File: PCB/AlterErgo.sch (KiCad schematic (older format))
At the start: 85 parts, among them SW0:10 SW_Push, SW0:11 SW_Push, SW0:12 SW_Push, SW0:7 SW_Push, SW0:8 SW_Push, SW0:9 SW_Push, SW1:10 SW_Push, SW1:11 SW_Push, SW1:12 SW_Push, SW1:13 SW_Push, SW1:7 SW_Push, SW1:8 SW_Push, SW1:9 SW_Push, SW2:10 SW_Push, SW2:11 SW_Push, SW2:12 SW_Push, SW2:13 SW_Push, SW2:7 SW_Push, SW2:8 SW_Push, SW2:9 SW_Push, SW3:10 SW_Push, SW3:11 SW_Push, SW3:12 SW_Push, SW3:13 SW_Push, SW3:8 SW_Push, SW3:9 SW_Push, SW4:10 SW_Push, SW4:11 SW_Push, SW4:12 SW_Push, SW4:13 SW_Push, SW4:7 SW_Push, SW4:8 SW_Push, SW4:9 SW_Push, SW5:10 SW_Push, SW5:11 SW_Push, SW5:12 SW_Push, SW5:13 SW_Push, SW5:7 SW_Push, SW5:8 SW_Push, SW5:9 SW_Push

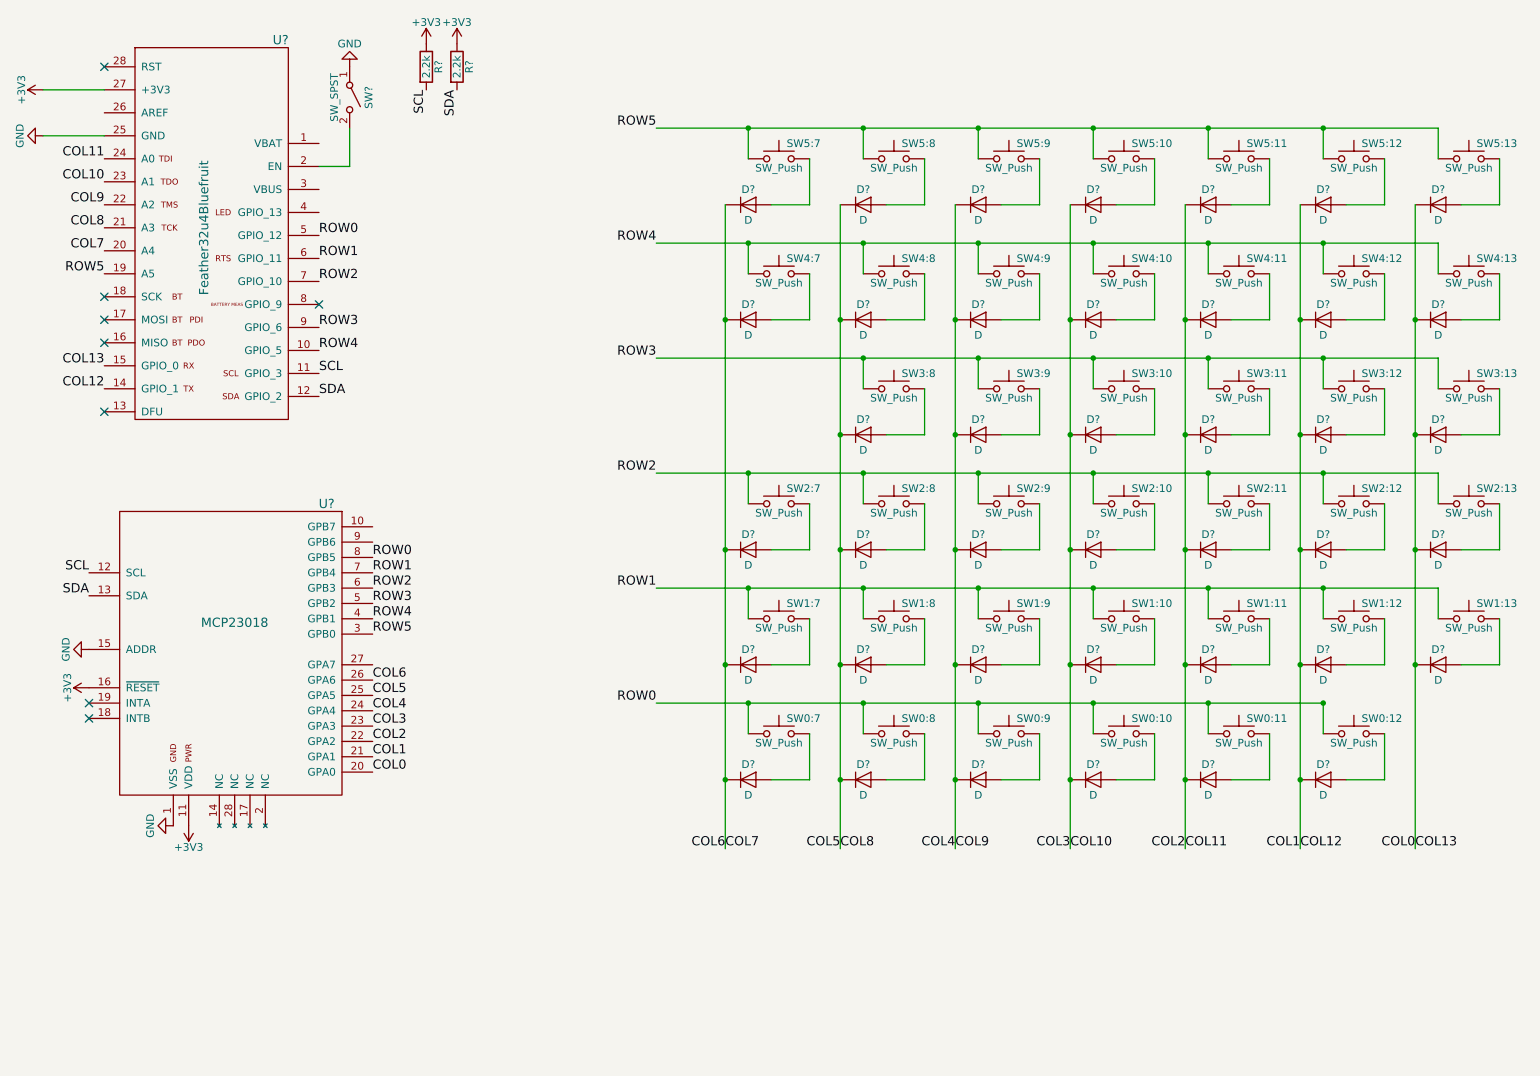
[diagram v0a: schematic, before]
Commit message: Add TRRS jack to schematic; annotate matrix diodes
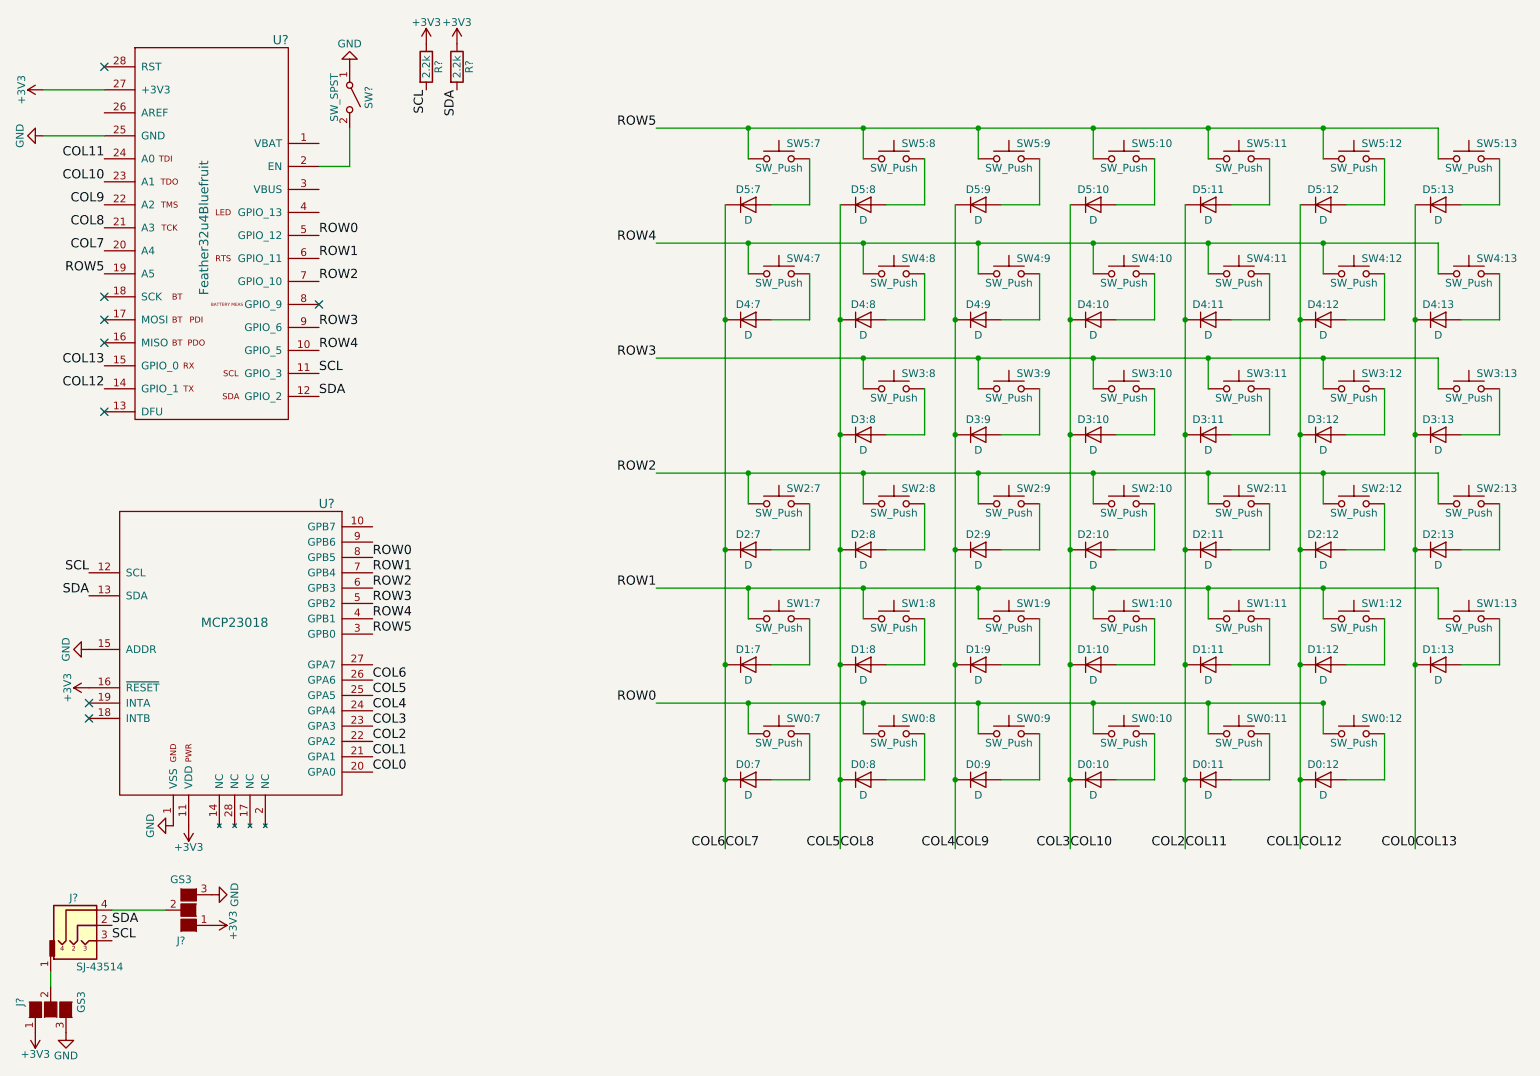
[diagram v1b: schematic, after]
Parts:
- added J?: SJ-43514, symbol SJ-43514
- added J? (x2): GS3, Connectors:GS3, symbol GS3
- gave numbers to parts that had none: 40
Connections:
- net +3V3: now also J?.1 (G1), J?.1 (G1)
- net GND: now also J?.3 (G3), J?.3 (G3)
- net SCL: now also J?.3
- net SDA: now also J?.2
- new net: J?.1, J?.2 (G2)
- new net: J?.2 (G2), J?.4

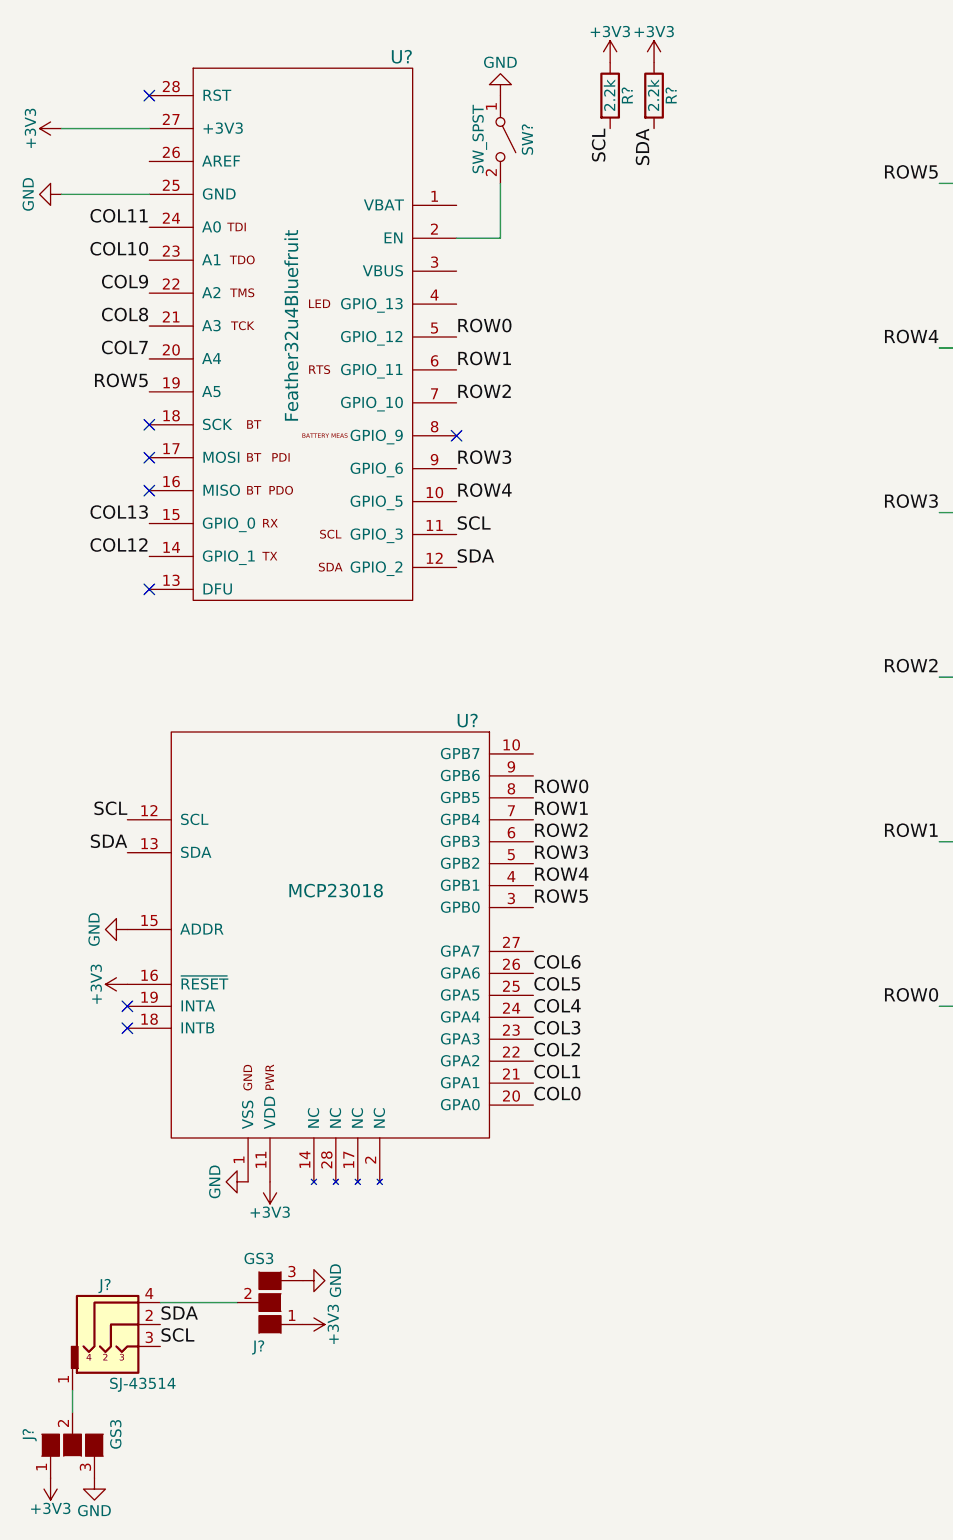
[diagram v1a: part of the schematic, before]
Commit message: Associate most components with footprints
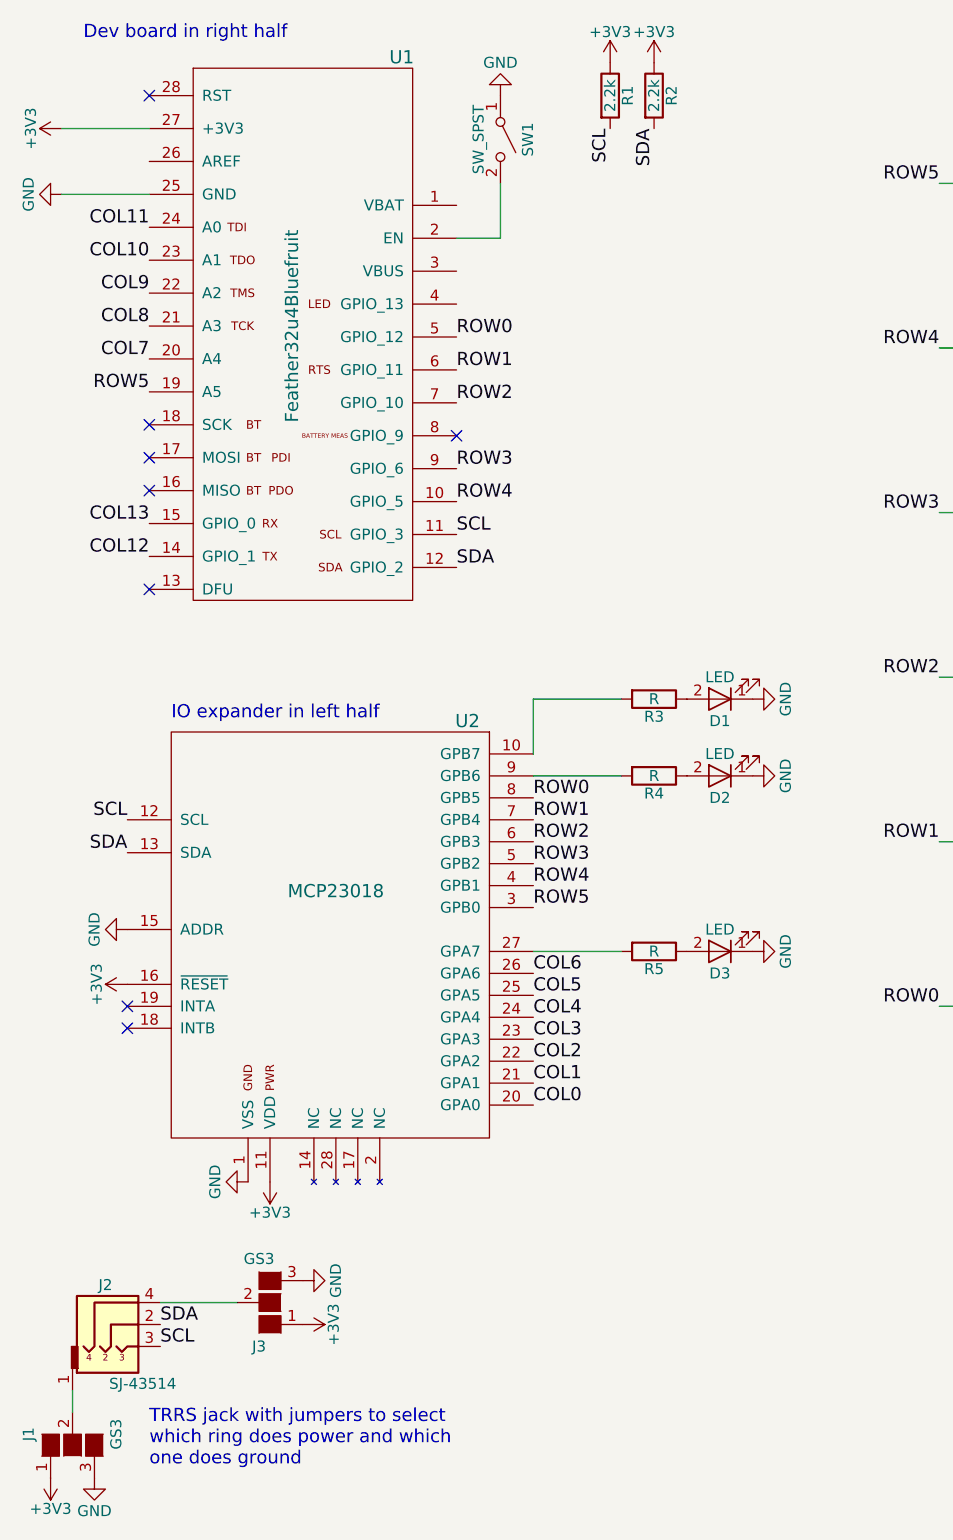
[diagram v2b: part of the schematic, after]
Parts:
- added D1, D2, D3: LED, LEDs:LED_D3.0mm, symbol LED
- added R3, R4, R5: R, Resistors_THT:R_Axial_DIN0207_L6.3mm_D2.5mm_P7.62mm_Horizontal, symbol R
- D0:10, D0:11, D0:12, D0:7, D0:8, D0:9, D1:10, D1:11, D1:12, D1:13, D1:7, D1:8, D1:9, D2:10, D2:11, D2:12, D2:13, D2:7, D2:8, D2:9, D3:10, D3:11, D3:12, D3:13, D3:8, D3:9, D4:10, D4:11, D4:12, D4:13, D4:7, D4:8, D4:9, D5:10, D5:11, D5:12, D5:13, D5:7, D5:8, D5:9: footprint (none) -> Diodes_SMD:D_SOD-123
- R1, R2: renamed from R?; footprint (none) -> Resistors_THT:R_Axial_DIN0207_L6.3mm_D2.5mm_P7.62mm_Horizontal
- SW1: renamed from SW?; footprint (none) -> keyboard_accessories:GPTS_SPST_Pushbutton
- U1: renamed from U?; footprint (none) -> keyboard_accessories:Feather32u4Bluefruit
- gave numbers to parts that had none: 4
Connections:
- net GND: now also D1.1 (K), D2.1 (K), D3.1 (K)
- net at U2.10 (GPB7): now also R3.2
- net at U2.27 (GPA7): now also R5.2
- net at U2.9 (GPB6): now also R4.2
- new net: D1.2 (A), R3.1
- new net: D2.2 (A), R4.1
- new net: D3.2 (A), R5.1
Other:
- note added: "Dev board in right half"
- note added: "IO expander in left half"
- note added: "TRRS jack with jumpers to select\nwhich ring does power and which\none does ground"

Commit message: Assign all components to footprints; generate netlist
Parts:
- J2: footprint (none) -> keyboard_accessories:TRRS_Jack_SJ-43514_reversible
- SW0:10, SW0:11, SW0:12, SW0:7, SW0:8, SW0:9, SW1:10, SW1:11, SW1:12, SW1:13, SW1:7, SW1:8, SW1:9, SW2:10, SW2:11, SW2:12, SW2:13, SW2:7, SW2:8, SW2:9, SW3:10, SW3:11, SW3:12, SW3:13, SW3:8, SW3:9, SW4:10, SW4:11, SW4:12, SW4:13, SW4:7, SW4:8, SW4:9, SW5:10, SW5:11, SW5:12, SW5:13, SW5:7, SW5:8, SW5:9: footprint (none) -> keyswitches:Kailh_socket_optional_reversible
- U2: footprint (none) -> Housings_DIP:DIP-28_W7.62mm

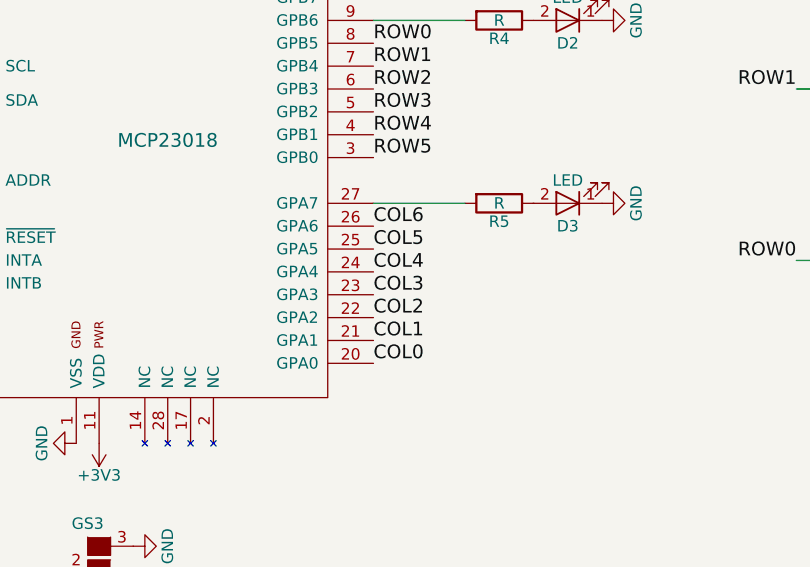
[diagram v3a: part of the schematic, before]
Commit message: Position non-angled switches on PCB
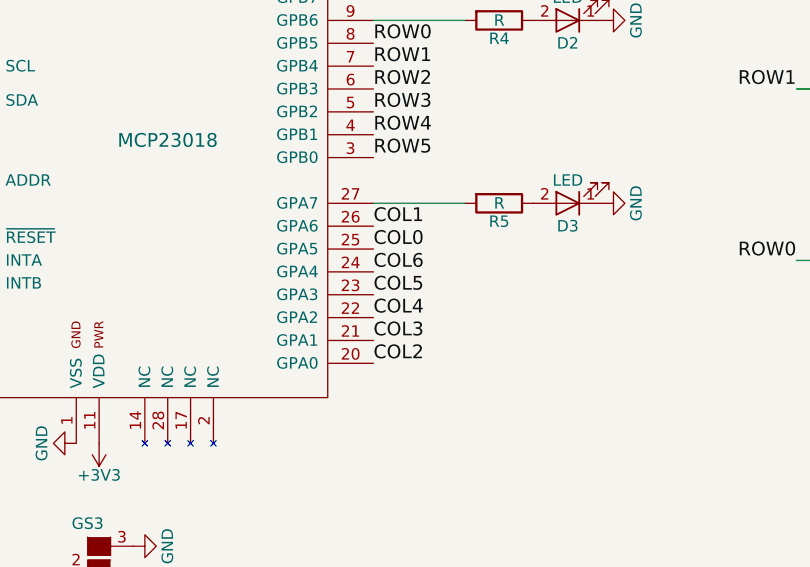
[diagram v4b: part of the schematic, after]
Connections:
- net COL0: now also U2.25 (GPA5); no longer U2.20 (GPA0)
- net COL1: now also U2.26 (GPA6); no longer U2.21 (GPA1)
- net COL10: now also U2.21 (GPA1); no longer U2.23 (GPA3)
- net COL11: now also U2.20 (GPA0); no longer U2.22 (GPA2)
- net COL4: now also U2.22 (GPA2); no longer U2.24 (GPA4)
- net COL5: now also U2.23 (GPA3); no longer U2.25 (GPA5)
- net COL6: now also U2.24 (GPA4); no longer U2.26 (GPA6)
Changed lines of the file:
@@
 Text Label 1450 2850 2    60   ~ 0
 COL13
+Text Label 3200 5000 0    60   ~ 0
+COL0
+Text Label 3200 4900 0    60   ~ 0
+COL1
 Text Label 3200 5500 0    60   ~ 0
-COL0
+COL2
 Text Label 3200 5400 0    60   ~ 0
-COL1
+COL3
 Text Label 3200 5300 0    60   ~ 0
-COL2
+COL4
 Text Label 3200 5200 0    60   ~ 0
-COL3
+COL5
 Text Label 3200 5100 0    60   ~ 0
-COL4
-Text Label 3200 5000 0    60   ~ 0
-COL5
-Text Label 3200 4900 0    60   ~ 0
 COL6
 Text Label 3200 4100 0    60   ~ 0
